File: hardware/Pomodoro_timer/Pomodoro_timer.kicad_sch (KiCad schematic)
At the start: 0 parts

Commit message: PCB Ver.A : The Schematic completed the next part for PCB can be started.
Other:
- added sheet MCU,Button,Buzzer (Power_Supply.kicad_sch)
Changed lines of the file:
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@@
+	)
+	(sheet
+		(at 17.78 82.55)
+		(size 76.2 46.99)
+		(exclude_from_sim no)
+		(in_bom yes)
+		(on_board yes)
+		(dnp no)
+		(fields_autoplaced yes)
+		(stroke
+			(width 0.1524)
+			(type solid)
+		)
+		(fill
+			(color 0 0 0 0.0000)
+		)
+		(property "Sheetname" "MCU,Button,Buzzer"
+			(at 17.78 81.8384 0)
+			(effects
+				(font
+					(size 1.27 1.27)
+				)
+				(justify left bottom)
+			)
+		)
+		(property "Sheetfile" "Power_Supply.kicad_sch"
+			(at 17.78 130.1246 0)
+			(effects
+				(font
+					(size 1.27 1.27)
+				)
+				(justify left top)
+			)
+		)
+		(instances
+			(project "Pomodoro_timer"
+				(path "/de804b87-618c-4b40-9e9d-dfdac3d4076a"
+					(page "4")
+				)
+			)
+		)
 	)
 	(sheet

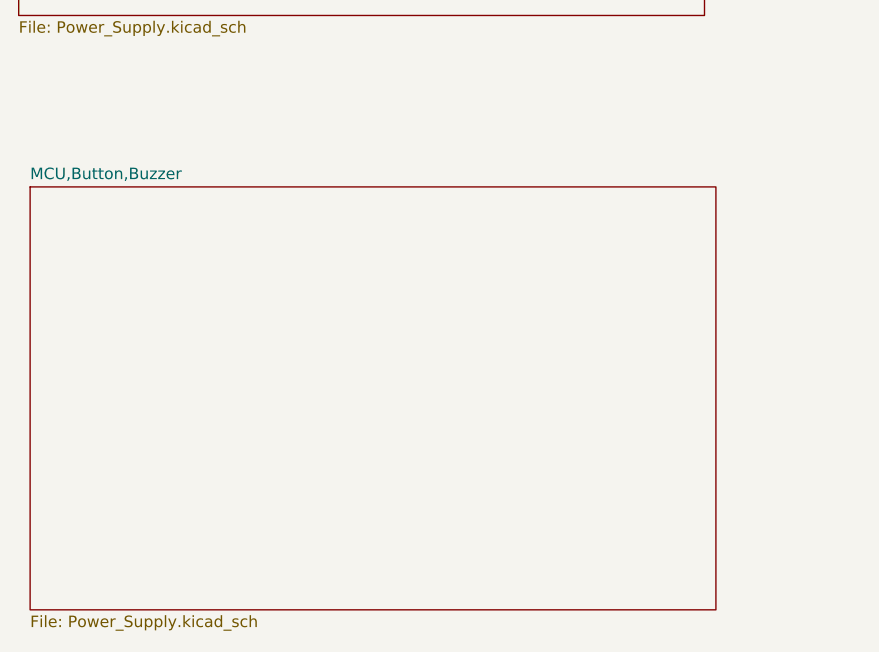
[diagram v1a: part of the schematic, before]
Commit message: PCB Ver.A The required changes were not in line So made few alterations Need to start again
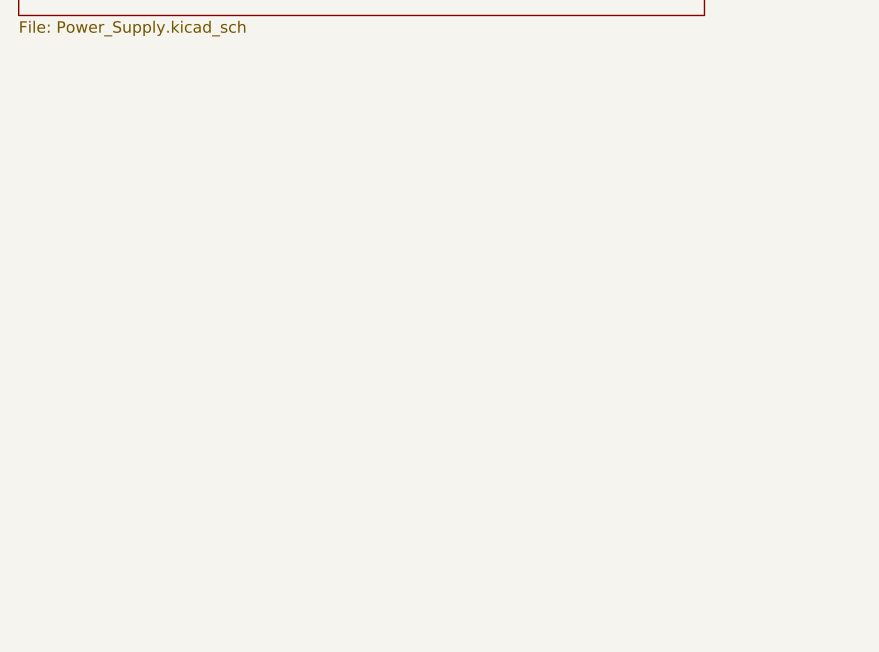
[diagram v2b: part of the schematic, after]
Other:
- removed sheet MCU,Button,Buzzer
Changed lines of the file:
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@@
-	)
-	(sheet
-		(at 17.78 82.55)
-		(size 76.2 46.99)
-		(exclude_from_sim no)
-		(in_bom yes)
-		(on_board yes)
-		(dnp no)
-		(fields_autoplaced yes)
-		(stroke
-			(width 0.1524)
-			(type solid)
-		)
-		(fill
-			(color 0 0 0 0.0000)
-		)
-		(property "Sheetname" "MCU,Button,Buzzer"
-			(at 17.78 81.8384 0)
-			(effects
-				(font
-					(size 1.27 1.27)
-				)
-				(justify left bottom)
-			)
-		)
-		(property "Sheetfile" "Power_Supply.kicad_sch"
-			(at 17.78 130.1246 0)
-			(effects
-				(font
-					(size 1.27 1.27)
-				)
-				(justify left top)
-			)
-		)
-		(instances
-			(project "Pomodoro_timer"
-				(path "/de804b87-618c-4b40-9e9d-dfdac3d4076a"
-					(page "4")
-				)
-			)
-		)
 	)
 	(sheet
